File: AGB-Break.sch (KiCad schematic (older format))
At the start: 39 parts, among them J1 CONN_WII, J2 Conn_02x03_Odd_Even, SW1 SW_Push, U1 AGB-CPU, U2 ATmega328P-AU, U3 TS5A3160DBV, U4 AGB_SRAM, U5 SpartanEdge, U6 LP5907MFX-2.5, U7 GBA-Slot, Y1 Crystal

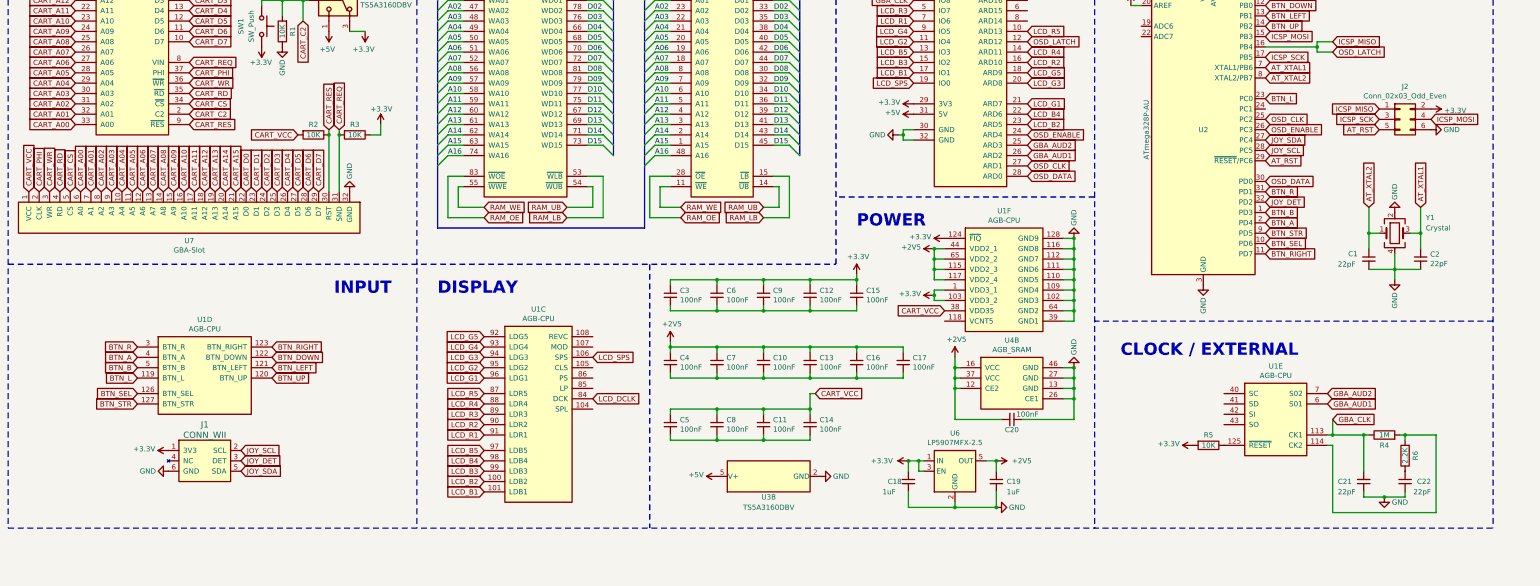
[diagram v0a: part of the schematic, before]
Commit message: Finished current routing, still missing power switch.
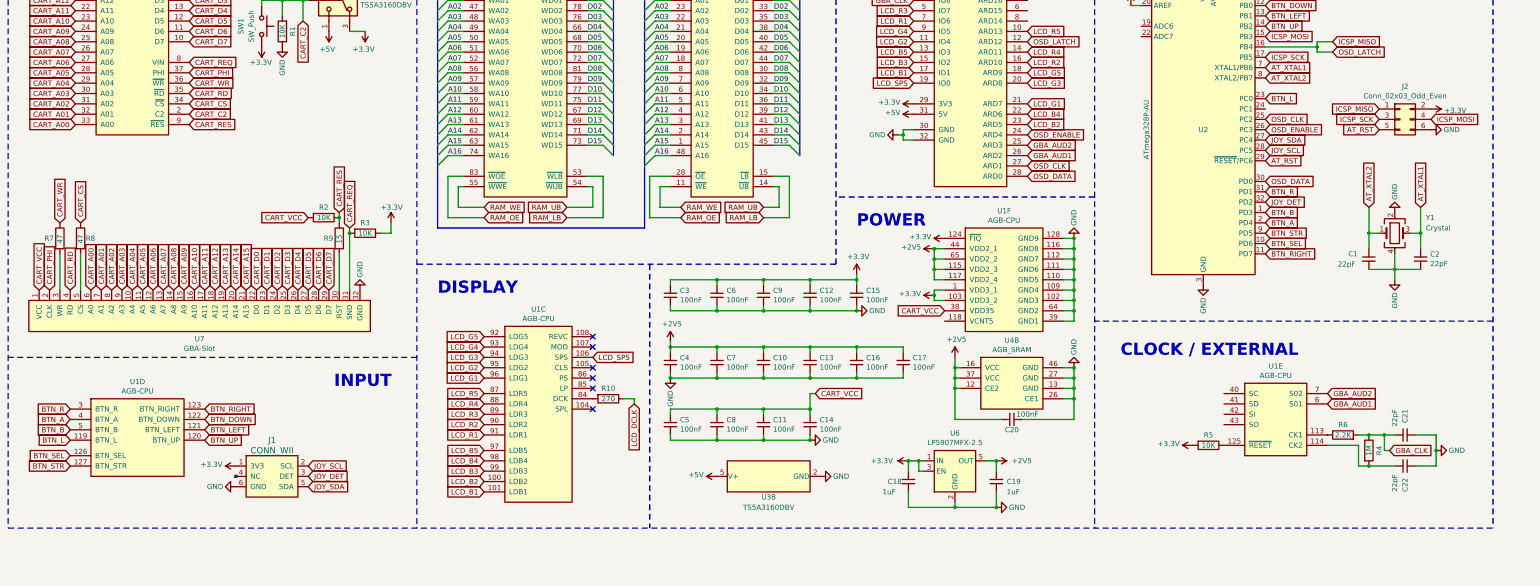
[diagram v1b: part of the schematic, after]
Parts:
- added R10: 270, Resistor_SMD:R_0805_2012Metric_Pad1.20x1.40mm_HandSolder, symbol Device:R
- added R7, R8: 47, Resistor_SMD:R_0805_2012Metric_Pad1.20x1.40mm_HandSolder, symbol Device:R
- added R9: 15, Resistor_SMD:R_0805_2012Metric_Pad1.20x1.40mm_HandSolder, symbol Device:R
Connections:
- net CART_CS: now also R8.1; no longer U7.5 (CS)
- net CART_RES: now also R9.1; no longer U7.30 (RST)
- net CART_WR: now also R7.1; no longer U7.3 (WR)
- net GBA_CLK: now also C21.1, R6.2; no longer C21.2, U1.113 (CK1)
- net GND: now also C10.2, C11.2, C12.2, C13.2, C14.2, C15.2, C16.2, C17.2, C21.2, C22.1, C3.2, C4.2, C5.2, C6.2, C7.2, C8.2, C9.2; no longer C21.1, C22.2
- net LCD_DCLK: now also R10.1; no longer U1.84 (DCK)
- net at R4.2, U1.114 (CK2): now also C22.2; no longer R6.2
- net at R6.1: now also U1.113 (CK1); no longer C22.1
- new net: R10.2, U1.84 (DCK)
- new net: R7.2, U7.3 (WR)
- new net: R9.2, U7.30 (RST)
- new net: R8.2, U7.5 (CS)
- no-connect marks 0 -> 6
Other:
- moved on the sheet: C21, C22, J1, R2, R3, R4, R6, U1D, U7

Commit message: Finished PCB v1
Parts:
- removed U2: ATmega328P-AU, Package_QFP:TQFP-32_7x7mm_P0.8mm, symbol MCU_Microchip_ATmega:ATmega328P-AU
- added D1: LED, LED_THT:LED_D5.0mm_FlatTop, symbol Device:LED
- added J3: Conn_01x02, Connector_PinSocket_2.54mm:PinSocket_1x02_P2.54mm_Vertical, symbol Connector_Generic:Conn_01x02
- added R11: 120, Resistor_SMD:R_0805_2012Metric_Pad1.20x1.40mm_HandSolder, symbol Device:R
- added U2: ATmega328PB-AU, Package_QFP:TQFP-32_7x7mm_P0.8mm, symbol MCU_Microchip_ATmega:ATmega328PB-AU
- added U8: Switch-DPDT, Raizu_OFFSET:XKB_XKB5858-Z-C, symbol Raizu:Switch-DPDT
- U4: footprint Gekkio_Package_SO:TSOP-I-48_16.4x12mm_P0.5mm -> Raizu_OFFSET:AGB_SRAM
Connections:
- net +3V3: now also U2.18 (AVCC), U2.20 (AREF), U2.4 (VCC)
- net AT_RST: now also U2.29 (~RESET~/PC6)
- net AT_XTAL1: now also U2.7 (XTAL1/PB6)
- net AT_XTAL2: now also U2.8 (XTAL2/PB7)
- net BTN_A: now also U2.2 (PD4)
- net BTN_B: now also U2.1 (PD3)
- net BTN_DOWN: now also U2.12 (PB0)
- net BTN_L: now also U2.23 (PC0)
- net BTN_LEFT: now also U2.13 (PB1)
- net BTN_R: now also U2.31 (PD1)
- net BTN_RIGHT: now also U2.11 (PD7)
- net BTN_SEL: now also U2.10 (PD6)
- net BTN_STR: now also U2.9 (PD5)
- net BTN_UP: now also U2.14 (PB2)
- net GND: now also R11.2, U2.21 (GND), U2.5 (GND)
- net ICSP_MISO: now also U2.16 (PB4)
- net ICSP_MOSI: now also U2.15 (PB3)
- net ICSP_SCK: now also U2.17 (PB5)
- net JOY_DET: now also U2.32 (PD2)
- net JOY_SCL: now also U2.28 (PC5)
- net JOY_SDA: now also U2.27 (PC4)
- net OSD_CLK: now also U2.25 (PC2)
- net OSD_DATA: now also U2.30 (PD0)
- net OSD_ENABLE: now also U2.26 (PC3)
- new net: D1.1 (K), R11.1
- new net PWR_5V: D1.2 (A), J3.1 (Pin_1), U8.3
- new net PWR_VIN: J3.2 (Pin_2), U8.2
- no-connect marks 6 -> 7
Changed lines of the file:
@@
-$EndComp
-$Comp
-L MCU_Microchip_ATmega:ATmega328P-AU U2
-U 1 1 617181FF
-P 12600 4650
-F 0 "U2" H 12600 4650 50  0000 C CNN
-F 1 "ATmega328P-AU" V 12050 4650 50  0000 C CNN
-F 2 "Package_QFP:TQFP-32_7x7mm_P0.8mm" H 12600 4650 50  0001 C CIN
-F 3 "http://ww1.microchip.com/downloads/en/DeviceDoc/ATmega328_P%20AVR%20MCU%20with%20picoPower%20Technology%20Data%20Sheet%2040001984A.pdf" H 12600 4650 50  0001 C CNN
-	1    12600 4650
-	1    0    0    -1
 $EndComp
 $Comp
@@
 F 0 "U4" H 7950 4165 50  0000 C CNN
 F 1 "AGB_SRAM" H 7950 4074 50  0000 C CNN
-F 2 "Gekkio_Package_SO:TSOP-I-48_16.4x12mm_P0.5mm" H 8200 3800 50  0001 C CNN
+F 2 "Raizu_OFFSET:AGB_SRAM" H 8200 3800 50  0001 C CNN
 F 3 "" H 8200 3800 50  0001 C CNN
 	1    7950 3600
@@
 F 0 "U4" H 10750 7715 50  0000 C CNN
 F 1 "AGB_SRAM" H 10750 7624 50  0000 C CNN
-F 2 "Gekkio_Package_SO:TSOP-I-48_16.4x12mm_P0.5mm" H 11000 7400 50  0001 C CNN
+F 2 "Raizu_OFFSET:AGB_SRAM" H 11000 7400 50  0001 C CNN
 F 3 "" H 11000 7400 50  0001 C CNN
 	2    10750 7200
@@
 Wire Wire Line
 	14850 7750 14850 7900
+$Comp
+L power:GND #PWR0134
+U 1 1 6118C0FD
+P 7450 7050
+F 0 "#PWR0134" H 7450 6800 50  0001 C CNN
+F 1 "GND" V 7450 6850 50  0000 C CNN
+F 2 "" H 7450 7050 50  0001 C CNN
+F 3 "" H 7450 7050 50  0001 C CNN
+	1    7450 7050
+	1    0    0    -1
+$EndComp
+Connection ~ 7450 7050
+$Comp
+L power:GND #PWR0135
+U 1 1 6118C952
+P 8800 7650
+F 0 "#PWR0135" H 8800 7400 50  0001 C CNN
+F 1 "GND" V 8800 7450 50  0000 C CNN
+F 2 "" H 8800 7650 50  0001 C CNN
+F 3 "" H 8800 7650 50  0001 C CNN
+	1    8800 7650
+	0    -1   -1   0
+$EndComp
+Connection ~ 8800 7650
+$Comp
+L power:GND #PWR0136
+U 1 1 6118CF2E
+P 9250 6400
+F 0 "#PWR0136" H 9250 6150 50  0001 C CNN
+F 1 "GND" V 9250 6200 50  0000 C CNN
+F 2 "" H 9250 6400 50  0001 C CNN
+F 3 "" H 9250 6400 50  0001 C CNN
+	1    9250 6400
+	0    -1   -1   0
+$EndComp
+Connection ~ 9250 6400
+$Comp
+L Raizu:Switch-DPDT U8
+U 1 1 60DFD4FD
+P 2200 8950
+F 0 "U8" H 2378 8951 50  0000 L CNN
+F 1 "Switch-DPDT" H 2378 8860 50  0000 L CNN
+F 2 "Raizu_OFFSET:XKB_XKB5858-Z-C" H 2200 8950 50  0001 C CNN
+F 3 "" H 2200 8950 50  0001 C CNN
+	1    2200 8950
+	1    0    0    -1
+$EndComp
+$Comp
+L Connector_Generic:Conn_01x02 J3
+U 1 1 60DFEF51
+P 1400 9100
+F 0 "J3" H 1318 8775 50  0000 C CNN
+F 1 "Conn_01x02" H 1318 8866 50  0000 C CNN
+F 2 "Connector_PinSocket_2.54mm:PinSocket_1x02_P2.54mm_Vertical" H 1400 9100 50  0001 C CNN
+F 3 "~" H 1400 9100 50  0001 C CNN
+	1    1400 9100
+	-1   0    0    1
+$EndComp
+Wire Wire Line
+	1600 9100 1700 9100
+$Comp
+L Device:LED D1
+U 1 1 60E3C677
+P 1950 9350
+F 0 "D1" H 1943 9567 50  0000 C CNN
+F 1 "LED" H 1943 9476 50  0000 C CNN
+F 2 "LED_THT:LED_D5.0mm_FlatTop" H 1950 9350 50  0001 C CNN
+F 3 "~" H 1950 9350 50  0001 C CNN
+	1    1950 9350
+	-1   0    0    1
+$EndComp
+$Comp
+L power:GND #PWR0137
+U 1 1 60E3CF15
+P 2400 9350
+F 0 "#PWR0137" H 2400 9100 50  0001 C CNN
+F 1 "GND" V 2400 9150 50  0000 C CNN
+F 2 "" H 2400 9350 50  0001 C CNN
+F 3 "" H 2400 9350 50  0001 C CNN
+	1    2400 9350
+	0    -1   -1   0
+$EndComp
+$Comp
+L Device:R R11
+U 1 1 60E3E7A2
+P 2250 9350
+F 0 "R11" V 2150 9350 50  0000 C CNN
+F 1 "120" V 2250 9350 50  0000 C CNN
+F 2 "Resistor_SMD:R_0805_2012Metric_Pad1.20x1.40mm_HandSolder" V 2180 9350 50  0001 C CNN
+F 3 "~" H 2250 9350 50  0001 C CNN
+	1    2250 9350
+	0    -1   -1   0
+$EndComp
+Wire Wire Line
+	1800 9350 1700 9350
+Wire Wire Line
+	1700 9350 1700 9100
+Connection ~ 1700 9100
+Text Label 1600 9100 0    50   ~ 0
+PWR_5V
+Text Label 1600 9000 0    50   ~ 0
+PWR_VIN
+Wire Wire Line
+	1600 9000 2050 9000
+Wire Wire Line
+	1700 9100 2050 9100
+NoConn ~ 2050 8900
 Wire Bus Line
 	5200 3400 5200 5600
@@
 	6900 2950 6900 4900
 $Comp
-L power:GND #PWR?
-U 1 1 6118C0FD
-P 7450 7050
-F 0 "#PWR?" H 7450 6800 50  0001 C CNN
-F 1 "GND" V 7450 6850 50  0000 C CNN
-F 2 "" H 7450 7050 50  0001 C CNN
-F 3 "" H 7450 7050 50  0001 C CNN
-	1    7450 7050
-	1    0    0    -1
-$EndComp
-Connection ~ 7450 7050
-$Comp
-L power:GND #PWR?
-U 1 1 6118C952
-P 8800 7650
-F 0 "#PWR?" H 8800 7400 50  0001 C CNN
-F 1 "GND" V 8800 7450 50  0000 C CNN
-F 2 "" H 8800 7650 50  0001 C CNN
-F 3 "" H 8800 7650 50  0001 C CNN
-	1    8800 7650
-	0    -1   -1   0
-$EndComp
-Connection ~ 8800 7650
-$Comp
-L power:GND #PWR?
-U 1 1 6118CF2E
-P 9250 6400
-F 0 "#PWR?" H 9250 6150 50  0001 C CNN
-F 1 "GND" V 9250 6200 50  0000 C CNN
-F 2 "" H 9250 6400 50  0001 C CNN
-F 3 "" H 9250 6400 50  0001 C CNN
-	1    9250 6400
-	0    -1   -1   0
-$EndComp
-Connection ~ 9250 6400
+L MCU_Microchip_ATmega:ATmega328PB-AU U2
+U 1 1 610ADD34
+P 12600 4650
+F 0 "U2" H 12600 4650 50  0000 C CNN
+F 1 "ATmega328PB-AU" V 12000 4650 50  0000 C CNN
+F 2 "Package_QFP:TQFP-32_7x7mm_P0.8mm" H 12600 4650 50  0001 C CIN
+F 3 "http://ww1.microchip.com/downloads/en/DeviceDoc/40001906C.pdf" H 12600 4650 50  0001 C CNN
+	1    12600 4650
+	1    0    0    -1
+$EndComp
 $EndSCHEMATC

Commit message: Finished PCB work, but headers are flipped, need to fix this :(
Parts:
- added C23: 100nF, Capacitor_SMD:C_0805_2012Metric_Pad1.18x1.45mm_HandSolder, symbol Device:C_Small
- added C24, C25, C26: 0.1nF, Capacitor_SMD:C_0805_2012Metric_Pad1.18x1.45mm_HandSolder, symbol Device:C_Small
- added EM1, EM2: EMI_Filter_3, Raizu_OFFSET:Inductor-1008-3P, symbol Raizu:EMI_Filter_3
- added J4: GameBoy_LinkPort, Gekkio_Connector:GameBoy_LinkPort_MGB_Horizontal, symbol Gekkio_Connector_Specialized:GameBoy_LinkPort
- added R12, R13, R14, R15: 330, Resistor_SMD:R_0805_2012Metric_Pad1.20x1.40mm_HandSolder, symbol Device:R
- added R?: 100k, Resistor_SMD:R_0805_2012Metric_Pad1.20x1.40mm_HandSolder, symbol Device:R
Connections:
- net CART_VCC: now also C23.1, J4.1 (VDD), R?.2
- net GND: now also C23.2, C24.2, C25.2, C26.2, EM1.1, EM1.6, EM2.3, EM2.4, J4.6 (GND), J4.SH
- net at U1.40 (SC): now also R12.1, R?.1
- net at U1.41 (SD): now also R13.1
- net at U1.42 (SI): now also R14.1
- net at U1.43 (SO): now also R15.1
- new net: EM1.2, J4.5 (SC)
- new net: C26.1, EM1.3, J4.4 (SD)
- new net: EM1.4, R13.2
- new net: EM1.5, R12.2
- new net: C24.1, EM2.1, J4.3 (SI)
- new net: C25.1, EM2.2, J4.2 (SO)
- new net: EM2.5, R15.2
- new net: EM2.6, R14.2
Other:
- note added: "LINK / AUDIO / CLOCK"
- note added: "SPARTAN POWER"
- note removed: "CLOCK / EXTERNAL"
- moved on the sheet: C1, C10, C11, C12, C13, C14, C15, C16, C17, C18, C19, C2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

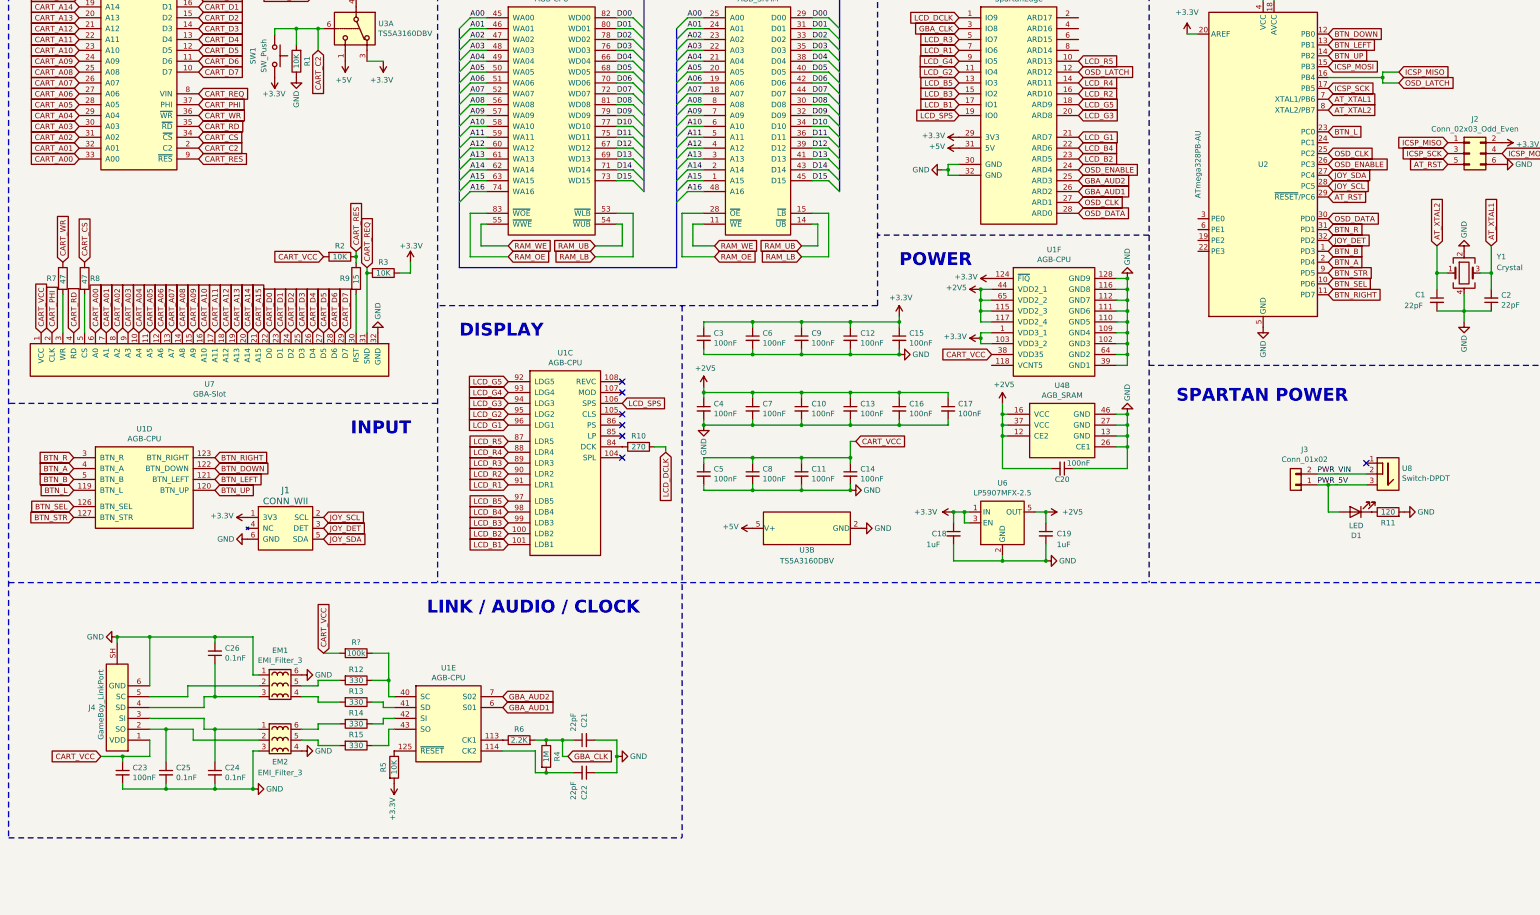
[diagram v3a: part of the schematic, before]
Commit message: Finished PCB layout, sent to pcb fab.
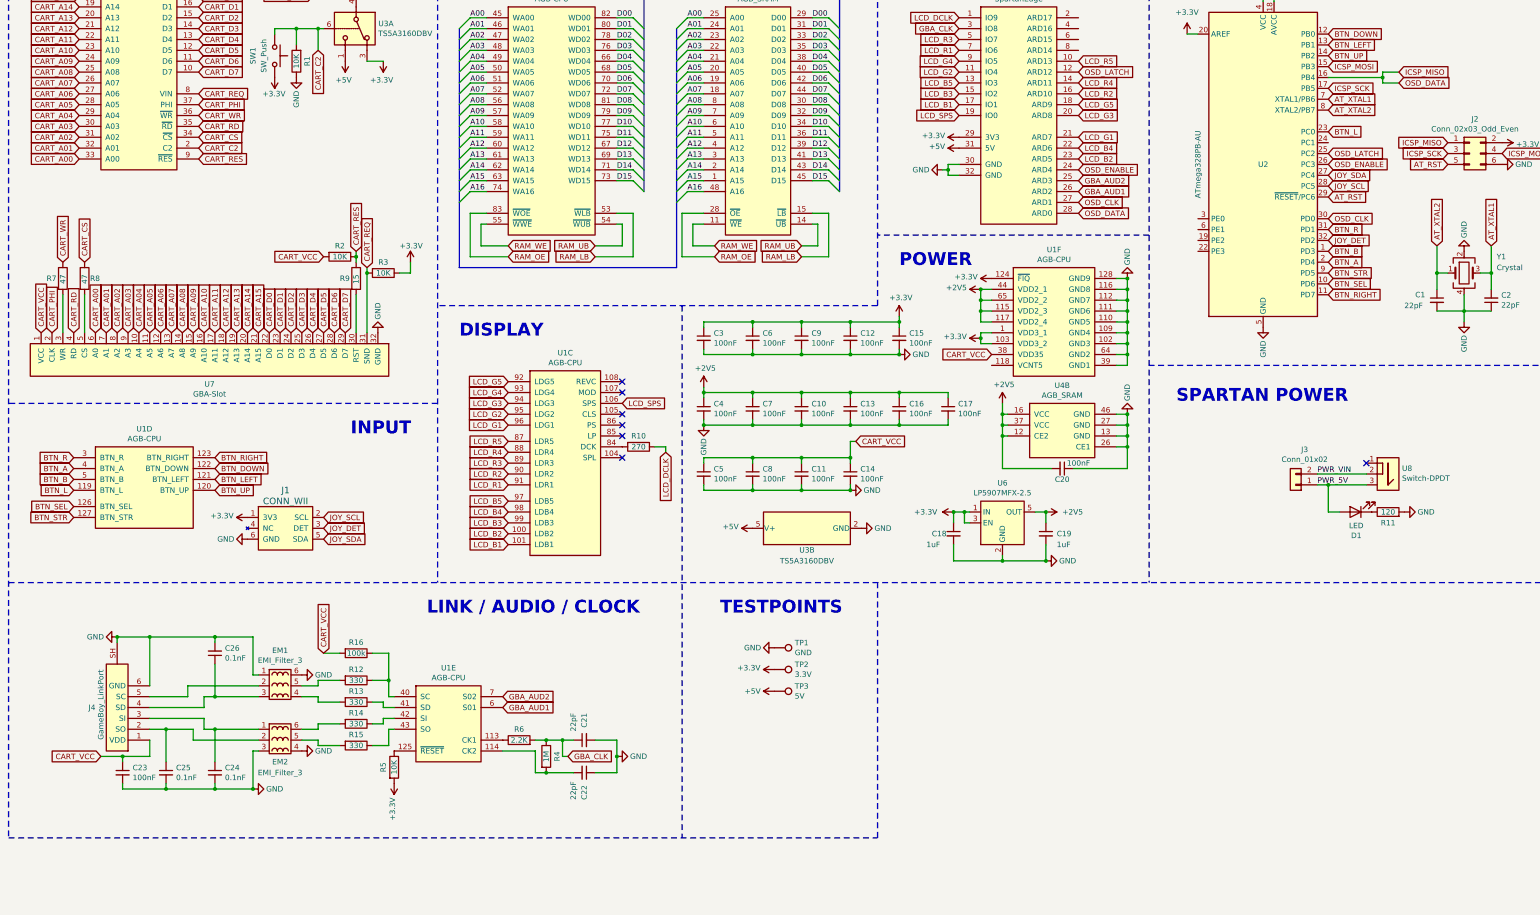
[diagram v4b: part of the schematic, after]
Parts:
- added TP1: GND, Raizu_OFFSET:SOLDER_PAD, symbol Connector:TestPoint
- added TP2: 3.3V, Raizu_OFFSET:SOLDER_PAD, symbol Connector:TestPoint
- added TP3: 5V, Raizu_OFFSET:SOLDER_PAD, symbol Connector:TestPoint
- gave numbers to parts that had none: 1
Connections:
- net +3V3: now also TP2.1
- net +5V: now also TP3.1
- net GND: now also TP1.1
- net ICSP_MISO: now also U5.28 (ARD0); no longer U5.12 (ARD12)
- net OSD_CLK: now also U2.30 (PD0); no longer U2.25 (PC2)
- removed net OSD_DATA: U2.30 (PD0), U5.28 (ARD0)
- new net OSD_LATCH: U2.25 (PC2), U5.12 (ARD12)
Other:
- note added: "TESTPOINTS"
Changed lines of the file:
@@
 	1    0    0    -1
 $EndComp
-Text GLabel 13150 4100 2    50   Input ~ 0
+Text GLabel 13800 2850 2    50   Input ~ 0
 OSD_DATA
-Text GLabel 13150 3500 2    50   Input ~ 0
-OSD_CLK
 Text GLabel 13150 3600 2    50   Input ~ 0
 OSD_ENABLE
@@
 Text GLabel 13800 2750 2    50   Input ~ 0
 ICSP_MISO
-Text GLabel 13800 2850 2    50   Input ~ 0
-OSD_LATCH
 Text GLabel 13150 2900 2    50   Input ~ 0
 ICSP_SCK
@@
 	2300 8900 2300 9050
 Wire Notes Line
-	1000 9800 7200 9800
-Wire Notes Line
 	7200 4900 7200 9800
 Wire Notes Line
@@
 	2300 7950 2900 7950
 $Comp
-L Device:R R?
+L Device:R R16
 U 1 1 61C5C1B1
 P 4200 8100
-F 0 "R?" V 4100 8100 50  0000 C CNN
+F 0 "R16" V 4100 8100 50  0000 C CNN
 F 1 "100k" V 4200 8100 50  0000 C CNN
 F 2 "Resistor_SMD:R_0805_2012Metric_Pad1.20x1.40mm_HandSolder" V 4130 8100 50  0001 C CNN
@@
 Wire Wire Line
 	4500 8100 4500 8350
+Text GLabel 13150 3500 2    50   Input ~ 0
+OSD_LATCH
+Text GLabel 13150 4100 2    50   Input ~ 0
+OSD_CLK
+$Comp
+L Connector:TestPoint TP1
+U 1 1 621A711A
+P 8050 8050
+F 0 "TP1" V 8004 8238 50  0000 L CNN
+F 1 "GND" V 8095 8238 50  0000 L CNN
+F 2 "Raizu_OFFSET:SOLDER_PAD" H 8250 8050 50  0001 C CNN
+F 3 "~" H 8250 8050 50  0001 C CNN
+	1    8050 8050
+	0    1    1    0
+$EndComp
+$Comp
+L Connector:TestPoint TP2
+U 1 1 621A794E
+P 8050 8250
+F 0 "TP2" V 8004 8438 50  0000 L CNN
+F 1 "3.3V" V 8095 8438 50  0000 L CNN
+F 2 "Raizu_OFFSET:SOLDER_PAD" H 8250 8250 50  0001 C CNN
+F 3 "~" H 8250 8250 50  0001 C CNN
+	1    8050 8250
+	0    1    1    0
+$EndComp
+$Comp
+L power:GND #PWR0142
+U 1 1 621A9C1E
+P 8050 8050
+F 0 "#PWR0142" H 8050 7800 50  0001 C CNN
+F 1 "GND" V 8050 7850 50  0000 C CNN
+F 2 "" H 8050 8050 50  0001 C CNN
+F 3 "" H 8050 8050 50  0001 C CNN
+	1    8050 8050
+	0    1    1    0
+$EndComp
+$Comp
+L Connector:TestPoint TP3
+U 1 1 621AA4F8
+P 8050 8450
+F 0 "TP3" V 8004 8638 50  0000 L CNN
+F 1 "5V" V 8095 8638 50  0000 L CNN
+F 2 "Raizu_OFFSET:SOLDER_PAD" H 8250 8450 50  0001 C CNN
+F 3 "~" H 8250 8450 50  0001 C CNN
+	1    8050 8450
+	0    1    1    0
+$EndComp
+$Comp
+L power:+3.3V #PWR0143
+U 1 1 621AAAD7
+P 8050 8250
+F 0 "#PWR0143" H 8050 8100 50  0001 C CNN
+F 1 "+3.3V" V 8065 8378 50  0000 L CNN
+F 2 "" H 8050 8250 50  0001 C CNN
+F 3 "" H 8050 8250 50  0001 C CNN
+	1    8050 8250
+	0    -1   -1   0
+$EndComp
+$Comp
+L power:+5V #PWR0144
+U 1 1 621AB3A7
+P 8050 8450
+F 0 "#PWR0144" H 8050 8300 50  0001 C CNN
+F 1 "+5V" V 8050 8650 50  0000 C CNN
+F 2 "" H 8050 8450 50  0001 C CNN
+F 3 "" H 8050 8450 50  0001 C CNN
+	1    8050 8450
+	0    -1   -1   0
+$EndComp
+Text Notes 7550 7750 0    118  ~ 24
+TESTPOINTS
+Wire Notes Line
+	9000 9800 9000 7450
+Wire Notes Line
+	1000 9800 9000 9800
 Wire Bus Line
 	5150 2350 5150 4550
